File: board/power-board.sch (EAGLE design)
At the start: 365 parts, among them J1 H1, J2 H2, J6 DF13-8P-1.25DS, J7 DF13-10P-1.25DS, J8 DF13-4P-1.25DS, J9 DF13-4P-1.25DS, Q1 TPC8120, Q2 TPC8120, Q3 SI7288, U1 INA214DCK, U10 INA214DCK, U11 INA214DCK, U12 INA214DCK, U13 MCP6561T-E/LT, U14 INA214DCK, U15 SN74AUP1G00DCK, U16 SN74LVC1G373DCK, U17 NTHD4508NT1, U18 MCP6561T-E/LT, U19 INA214DCK, U2 INA214DCK, U20 SN74AUP1G00DCK, U21 SN74LVC1G373DCK, U22 NTHD4508NT1, U23 MCP6561T-E/LT, U24 INA214DCK, U25 SN74AUP1G00DCK, U26 SN74LVC1G373DCK, U27 NTHD4508NT1, U28 MCP6561T-E/LT, U29 INA214DCK, U3 INA214DCK, U30 SN74AUP1G00DCK, U31 SN74LVC1G373DCK, U32 NTHD4508NT1, U33 MCP6561T-E/LT, U34 INA214DCK, U35 SN74AUP1G00DCK, U36 SN74LVC1G373DCK, U37 NTHD4508NT1, U38 MCP6561T-E/LT, U39 INA214DCK, U4 INA214DCK, U40 SN74AUP1T08DCK, U41 SN74LVC1G373DCK, U42 FDS8858CZ, U43 TLV3491AIDBV, U44 TPS62132RGT, U45 FDS8858CZ, U46 TLV3491AIDBV, U47 TPS62133RGT, U48 FDS8858CZ, U49 MSP430F2132, U5 INA214DCK, U50 ADG732, U51 SPV1040T, U52 SPV1040T, U53 BQ24650_RVA_16, U54 INA214DCK, U6 INA214DCK, U7 INA214DCK, U8 INA214DCK, U9 INA214DCK, X1 32.768k

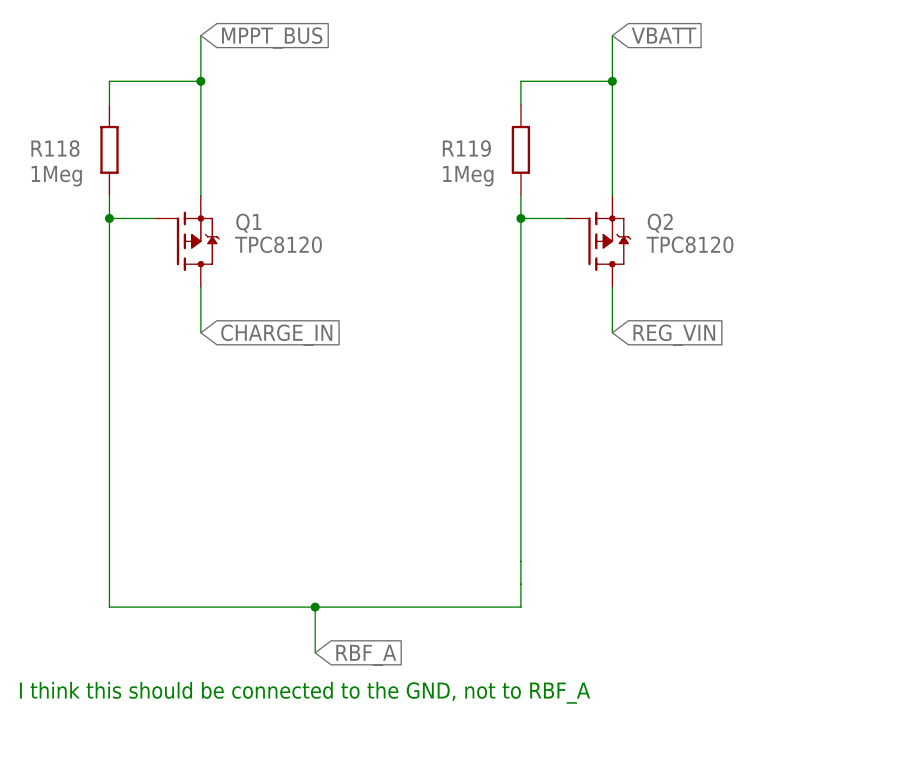
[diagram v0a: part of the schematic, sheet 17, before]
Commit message: removing deployment switches, adding testpoints
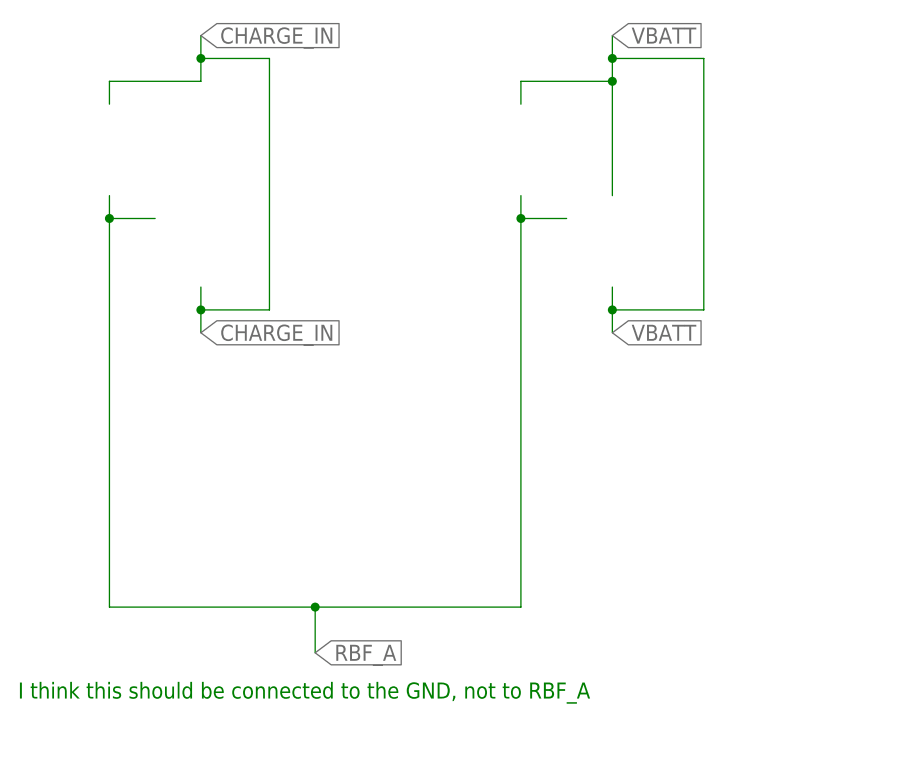
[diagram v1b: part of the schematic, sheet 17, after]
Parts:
- removed Q1, Q2: TPC8120, gdp_pss_library:TPC8120
- removed R118, R119: 1Meg, rcl:R-EU_R0603
- added FID1, FID2, FID3, FID4: FIDUCIAL1X2-STOP, fiducial:FIDUCIAL1X2-STOP
- added TP1, TP10, TP11, TP12, TP13, TP14, TP2, TP3, TP4, TP5, TP6, TP7, TP8, TP9: PTR1TP09R, testpad:PTR1TP09R
- R39: value 442m -> 50m
- R48: value 43m -> 124m
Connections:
- net 3V3_BU_RADIO renamed 5V_TX_RADIO
- removed net MPPT_BUS: C122.1, Q1.S, R113.1, R116.1, R118.2, R31.2
- removed net REG_VIN: C100.1, C104.1, C106.1, C107.1, C95.1, C97.1, C99.1, J2.20, Q2.D, R102.1, R37.2, R44.2, R53.2, R62.2, R71.2, R80.2, R84.1, R95.1, U39.IN+, U44.AVIN, U44.EN, U44.PVIN, U47.AVIN, U47.EN, U47.PVIN
- new net 5V_RX_RADIO: C53.1, R55.2, U22A.S
- net 3V3_RADIO: no longer C53.1, R55.2, U22A.S
- net CHARGE_IN: now also C122.1, R113.1, R116.1, R31.2; no longer Q1.D
- net OCP1_COMP_OUT: now also TP12.TP
- net OCP1_MCU_EN: now also TP11.TP
- net OCP1_SENSEM: now also R44.2
- net OCP2_COMP_OUT: now also TP10.TP
- net OCP2_MCU_EN: now also TP9.TP
- net OCP2_SENSEM: now also R53.2
- net OCP3_COMP_OUT: now also TP8.TP
- net OCP3_MCU_EN: now also TP7.TP
- net OCP3_SENSEM: now also R62.2
- net OCP4_COMP_OUT: now also TP6.TP
- net OCP4_MCU_EN: now also TP5.TP
- net OCP4_SENSEM: now also R71.2
- net OCP5_COMP_OUT: now also TP4.TP
- net OCP5_MCU_EN: now also TP3.TP
- net OCP5_SENSEM: now also R80.2
- net OCP6_COMP_OUT: now also TP2.TP
- net OCP6_MCU_EN: now also TP1.TP
- net RBF_A: no longer Q1.G, Q2.G, R118.1, R119.1
- net UVP3V3_GATE: now also TP13.TP
- net UVP3V3_OUT: no longer R39.1, R48.1, U14.IN+, U19.IN+
- net UVP5V_GATE: now also TP14.TP
- net UVP5V_OUT: now also R39.1, R48.1, U14.IN+, U19.IN+
- net VBATT: now also C100.1, C104.1, C106.1, C107.1, C95.1, C97.1, C99.1, J2.20, R102.1, R37.2, R84.1, R95.1, U39.IN+, U44.AVIN, U44.EN, U44.PVIN, U47.AVIN, U47.EN, U47.PVIN; no longer Q2.S, R119.2

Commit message: done (hopefully)
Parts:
- added TP15, TP16, TP17, TP18, TP19, TP20, TP21, TP22, TP23, TP24, TP25, TP26, TP27, TP28, TP29, TP30: PTR1TP09R, testpad:PTR1TP09R
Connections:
- removed net 3V3_RADIO: J1.51
- net 3V3_FLIGHT_MCU: now also TP24.TP
- net 3V3_SYS: now also TP16.TP
- net 5V_CAMERA: now also TP25.TP
- net 5V_RX_RADIO: now also J1.51, TP26.TP
- net 5V_SYS: now also TP15.TP
- net 5V_TX_RADIO: now also TP27.TP
- net CHARGE_IN: now also TP28.TP
- net GND: now also TP30.TP
- net MPPT2_OUT: now also TP29.TP
- net OCP1_SENSEM: no longer R44.2
- net OCP2_SENSEM: no longer R53.2
- net OCP3_SENSEM: no longer R62.2
- net OCP4_SENSEM: no longer R71.2
- net OCP5_SENSEM: no longer R80.2
- net OEM615_3V3: now also TP23.TP
- net OEM615_LNA_PWR: now also TP22.TP
- net REG3V3: now also TP21.TP
- net REG5V: now also TP20.TP
- net UVP3V3_OUT: now also TP17.TP; no longer C40.1, C51.1
- net UVP5V_OUT: now also C40.1, C51.1, TP18.TP
- net VBATT: now also R44.2, R53.2, R62.2, R71.2, R80.2, TP19.TP

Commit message: committing WIP
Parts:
- added C143, C148, C153, C158: 1u, rcl:C-EUC0603K
- added C144, C149, C154, C159: 100n, rcl:C-EUC0603K
- added C145, C146, C150, C151, C155, C156, C160, C161: 10u, rcl:C-EUC0805K
- added C147, C152, C157, C162: 4.7u, rcl:C-EUC0805K
- added D12, D13, D14, D15: 5V1, diode:SUPPRESSOR-SMBJ
- added L6, L7, L8, L9: 10uH, gdp_pss_library:MSS7341
- added R118, R119, R143, R144, R145, R147, R148, R149, R151, R152, R153, R155: 1k, rcl:R-EU_R0603
- added R142, R146, R150, R154: 10m, rcl:R-EU_R1206
- added TP31, TP32, TP33, TP34, TP35, TP36: PTR1TP09R, testpad:PTR1TP09R
- added U55, U56, U57, U58: SPV1040T, gdp_pss_library:SPV1040T
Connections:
- net MPPT2_OUT renamed MPPT1_MID
- new net MPPT1H_PV_P: C114.1, L3.1, R110.1
- new net MPPT1L_PV_P: C115.1, L4.1, R111.1
- new net MPPT2H_PV_P: C146.1, L6.1, R143.1
- new net MPPT2L_PV_P: C151.1, L7.1, R147.1
- new net MPPT2_MID: C144.2, C145.2, C146.2, C147.2, C150.1, D12.A, R145.1, R146.1, TP32.TP, U55.GND, U55.VCTRL
- new net MPPT3H_PV_P: C156.1, L8.1, R151.1
- new net MPPT3L_PV_P: C161.1, L9.1, R155.1
- new net MPPT3_MID: C154.2, C155.2, C156.2, C157.2, C160.1, D14.A, R153.1, R154.1, TP35.TP, U57.GND, U57.VCTRL
- new net N$778: C144.1, R143.2, U55.MPP-SET, U55.XSHUT
- new net N$779: L6.2, U55.LX
- new net N$780: C148.1, R144.2, U56.ICTRL+
- new net N$781: C148.2, R145.2, U56.ICTRL-
- new net N$782: C152.1, D13.C, R144.1, R146.2, U56.VOUT
- new net N$783: C149.1, R147.2, U56.MPP-SET, U56.XSHUT
- new net N$784: L7.2, U56.LX
- new net N$785: C153.1, R148.2, U57.ICTRL+
- new net N$786: C153.2, R149.2, U57.ICTRL-
- new net N$787: C157.1, D14.C, R148.1, R150.2, U57.VOUT
- new net N$788: C154.1, R151.2, U57.MPP-SET, U57.XSHUT
- new net N$789: L8.2, U57.LX
- new net N$790: C158.1, R152.2, U58.ICTRL+
- new net N$791: C158.2, R153.2, U58.ICTRL-
- new net N$792: C162.1, D15.C, R152.1, R154.2, U58.VOUT
- new net N$793: C159.1, R155.2, U58.MPP-SET, U58.XSHUT
- new net N$794: L9.2, U58.LX
- new net N$89: C143.1, R118.2, U55.ICTRL+
- new net N$91: C143.2, R119.2, U55.ICTRL-
- new net N$92: C147.1, D12.C, R118.1, R142.2, U55.VOUT
- net CHARGE_IN: now also C145.1, C155.1, R119.1, R142.1, R149.1, R150.1, TP31.TP, TP34.TP
- net GND: now also C149.2, C150.2, C151.2, C152.2, C159.2, C160.2, C161.2, C162.2, D13.A, D15.A, TP33.TP, TP36.TP, U56.GND, U56.VCTRL, U58.GND, U58.VCTRL
- net MPPT1_PV_P: no longer C114.1, L3.1, R110.1
- net MPPT2_PV_P: no longer C115.1, L4.1, R111.1
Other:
- note added: "< WHY?"
- note added: "MPPT 1H"
- note added: "MPPT 1L"
- note added: "MPPT 2H"
- note added: "MPPT 2L"
- note added: "MPPT 3H"
- note added: "MPPT 3L"
- note added: "review all these connections"
- note added: "wire thse SWD pins"
- moved on the sheet: C114, C115, C116, C117, C118, C119, C120, C121, C122, C123, D7, D8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

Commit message: various bits of routing over a period of time
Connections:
- net MPPT1H_PV_P: now also R6.2, R9.2, U4.IN-, U5.IN-
- net MPPT1L_PV_P: now also R16.2, R19.2, U10.IN-, U9.IN-
- net MPPT1_MID: no longer J2.16, J2.8, J9.2
- net MPPT1_PV_P: no longer R10.2, R13.2, R5.2, R6.2, R9.2, U3.IN-, U4.IN-, U5.IN-, U6.IN-, U7.IN-
- net MPPT2H_PV_P: now also R10.2, R13.2, U6.IN-, U7.IN-
- net MPPT2L_PV_P: now also R20.2, R23.2, U11.IN-, U12.IN-
- net MPPT2_MID: now also J2.16, J9.2
- net MPPT2_PV_P: no longer R15.2, R16.2, R19.2, R20.2, R23.2, U10.IN-, U11.IN-, U12.IN-, U8.IN-, U9.IN-
- net MPPT3H_PV_P: now also R5.2, U3.IN-
- net MPPT3L_PV_P: now also R15.2, U8.IN-
- net MPPT3_MID: now also J2.8
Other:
- note added: "1 +"
- note added: "1 -"
- note added: "2 +"
- note added: "2 -"
- note added: "east pv 1 +"
- note added: "east pv 1 -"
- note added: "east pv 2 +"
- note added: "east pv 2 -"
- note added: "east/west"
- note added: "north/south"
- note added: "top"
- note added: "top pv 1 +"
- note added: "top pv 1 -"
- note added: "top pv 2 +"
- note added: "top pv 2 -"
- note removed: "< WHY?"

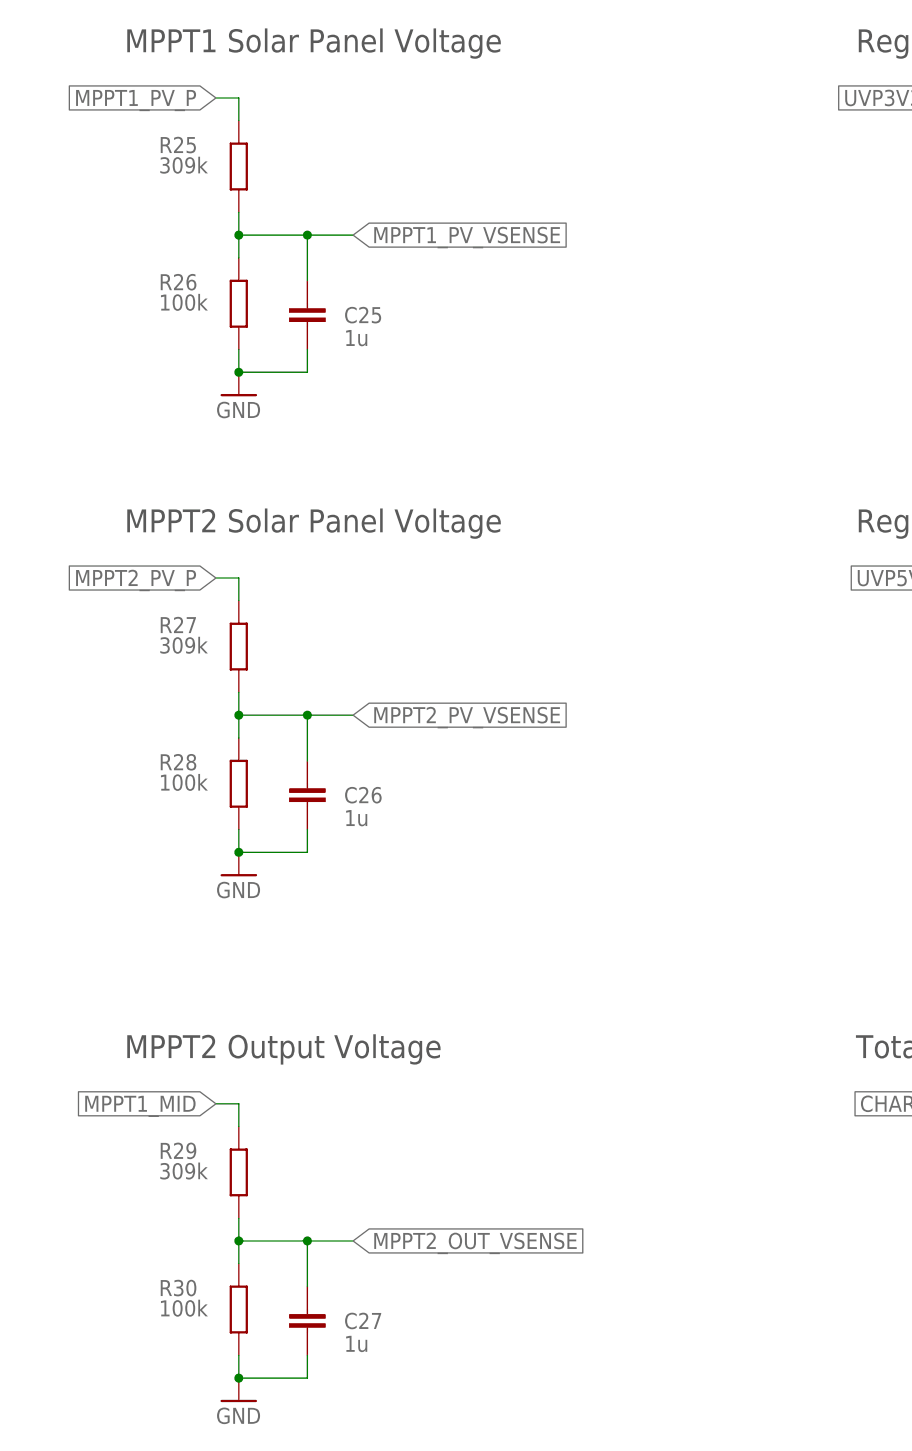
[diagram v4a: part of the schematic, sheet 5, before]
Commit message: changing mppt voltage monitoring points
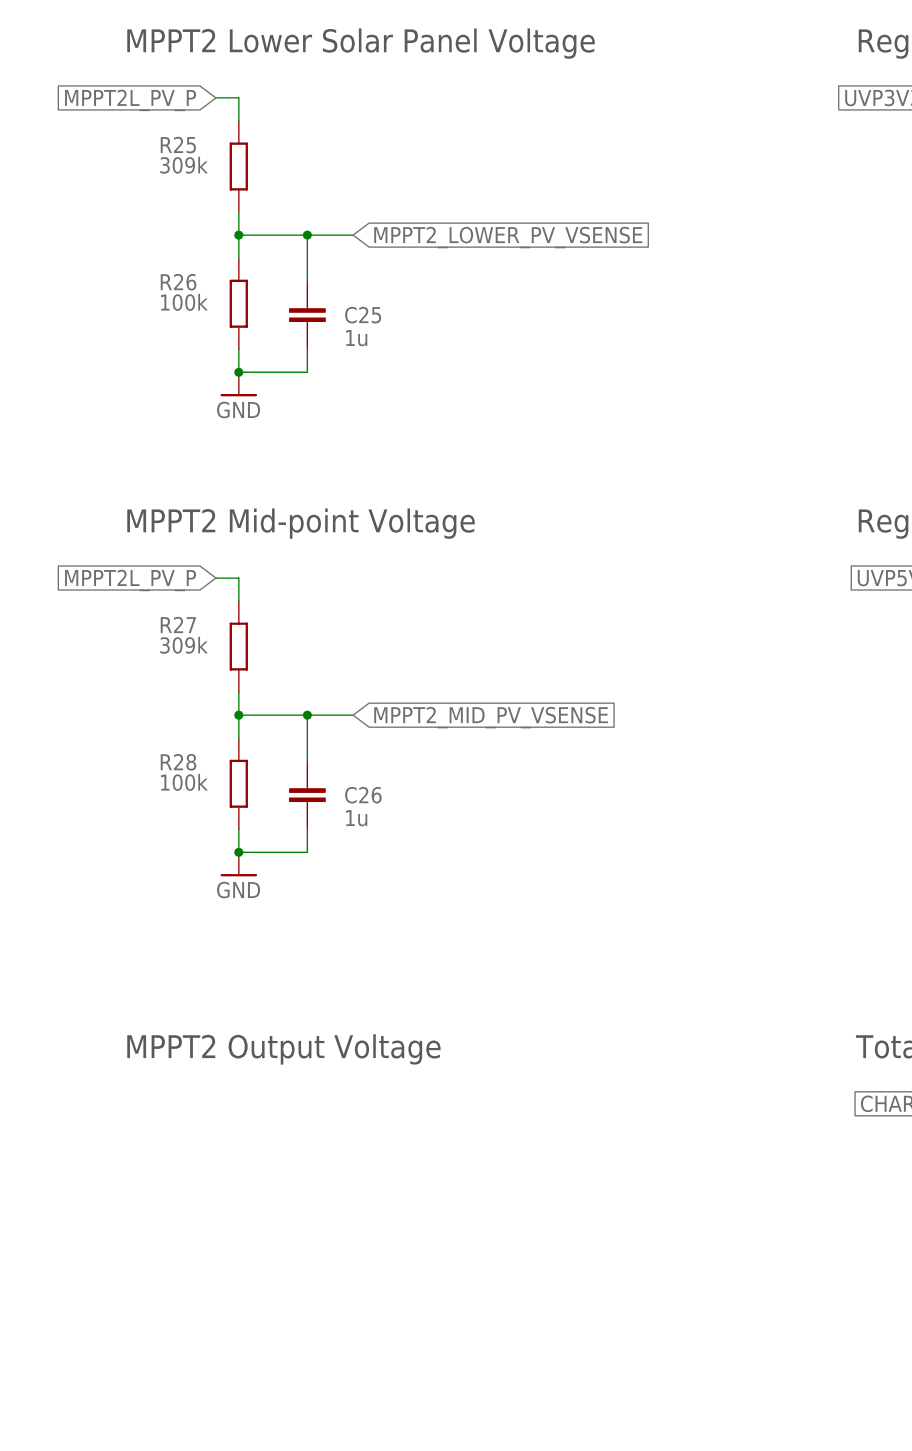
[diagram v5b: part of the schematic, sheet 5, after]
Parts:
- removed C27: 1u, rcl:C-EUC0603
- removed R29: 309k, rcl:R-EU_R0603
- removed R30: 100k, rcl:R-EU_R0603
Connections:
- net MPPT1_PV_VSENSE renamed MPPT2_LOWER_PV_VSENSE
- net MPPT2_PV_VSENSE renamed MPPT2_MID_PV_VSENSE
- removed net MPPT1_PV_P: R25.2
- removed net MPPT2_OUT_VSENSE: C27.1, R29.1, R30.2
- removed net MPPT2_PV_P: R27.2
- net GND: no longer C27.2, R30.1
- net MPPT1_MID: no longer R29.2
- net MPPT2L_PV_P: now also R25.2, R27.2
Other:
- note added: "MPPT2 Lower Solar Panel Voltage"
- note added: "MPPT2 Mid-point Voltage"
- note removed: "MPPT1 Solar Panel Voltage"
- note removed: "MPPT2 Solar Panel Voltage"
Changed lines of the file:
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@@
 <?xml version="1.0" encoding="utf-8"?>
 <!DOCTYPE eagle SYSTEM "eagle.dtd">
-<eagle version="7.6.0">
+<eagle version="9.0.1">
 <drawing>
 <settings>
-<setting alwaysvectorfont="yes"/>
+<setting alwaysvectorfont="no"/>
+<setting keepoldvectorfont="yes"/>
 <setting verticaltext="up"/>
 </settings>
@@
 <part name="C19" library="rcl" deviceset="C-EU" device="C0603" value="100n"/>
 <part name="GND23" library="supply1" deviceset="GND" device=""/>
-<part name="R29" library="rcl" deviceset="R-EU_" device="R0603" value="309k"/>
-<part name="R30" library="rcl" deviceset="R-EU_" device="R0603" value="100k"/>
-<part name="GND31" library="supply1" deviceset="GND" device=""/>
 <part name="R21" library="rcl" deviceset="R-EU_" device="R0603" value="10k"/>
 <part name="C21" library="rcl" deviceset="C-EU" device="C0603" value="1u"/>
 <part name="GND25" library="supply1" deviceset="GND" device=""/>
-<part name="C27" library="rcl" deviceset="C-EU" device="C0603" value="1u"/>
 <part name="J7" library="con-hirose-df13" deviceset="DF13-10P-1.25" device="DS"/>
 <part name="J6" library="con-hirose-df13" deviceset="DF13-8P-1.25" device="DS"/>
@@
 <description>Voltage Measurements</description>
 <plain>
-<text x="27.94" y="162.56" size="2.54" layer="97">MPPT1 Solar Panel Voltage</text>
-<text x="27.94" y="109.22" size="2.54" layer="97">MPPT2 Solar Panel Voltage</text>
+<text x="27.94" y="162.56" size="2.54" layer="97">MPPT2 Lower Solar Panel Voltage</text>
+<text x="27.94" y="109.22" size="2.54" layer="97">MPPT2 Mid-point Voltage</text>
 <text x="109.22" y="109.22" size="2.54" layer="97">Regulated 5V After UVP Switch</text>
 <text x="109.22" y="162.56" size="2.54" layer="97">Regulated 3V3 After UVP Switch</text>
@@
 </instance>
 <instance part="FRAME5" gate="G$1" x="0" y="0"/>
-<instance part="R29" gate="G$1" x="40.64" y="38.1" smashed="yes" rot="R90">
-<attribute name="NAME" x="31.75" y="39.5986" size="1.778" layer="95"/>
-<attribute name="VALUE" x="31.75" y="37.338" size="1.778" layer="96"/>
-</instance>
-<instance part="R30" gate="G$1" x="40.64" y="22.86" smashed="yes" rot="R90">
-<attribute name="NAME" x="31.75" y="24.3586" size="1.778" layer="95"/>
-<attribute name="VALUE" x="31.75" y="22.098" size="1.778" layer="96"/>
-</instance>
-<instance part="GND31" gate="1" x="40.64" y="12.7"/>
-<instance part="C27" gate="G$1" x="48.26" y="22.86" smashed="yes">
-<attribute name="NAME" x="52.324" y="20.701" size="1.778" layer="95"/>
-<attribute name="VALUE" x="52.324" y="18.161" size="1.778" layer="96"/>
-</instance>
 <instance part="R31" gate="G$1" x="127" y="38.1" smashed="yes" rot="R90">
 <attribute name="NAME" x="118.11" y="39.5986" size="1.778" layer="95"/>
@@
 </segment>
 <segment>
-<pinref part="GND31" gate="1" pin="GND"/>
-<pinref part="R30" gate="G$1" pin="1"/>
-<wire x1="40.64" y1="15.24" x2="40.64" y2="17.78" width="0.1524" layer="91"/>
-<pinref part="C27" gate="G$1" pin="2"/>
-<wire x1="48.26" y1="17.78" x2="48.26" y2="15.24" width="0.1524" layer="91"/>
-<wire x1="48.26" y1="15.24" x2="40.64" y2="15.24" width="0.1524" layer="91"/>
-<junction x="40.64" y="15.24"/>
-</segment>
-<segment>
 <pinref part="GND32" gate="1" pin="GND"/>
 <pinref part="R32" gate="G$1" pin="1"/>
@@
 </segment>
 </net>
-<net name="MPPT1_PV_P" class="0">
-<segment>
-<label x="38.1" y="157.48" size="1.778" layer="95" rot="R180" xref="yes"/>
-<pinref part="R25" gate="G$1" pin="2"/>
-<wire x1="40.64" y1="157.48" x2="38.1" y2="157.48" width="0.1524" layer="91"/>
-<wire x1="40.64" y1="154.94" x2="40.64" y2="157.48" width="0.1524" layer="91"/>
-</segment>
-</net>
-<net name="MPPT1_PV_VSENSE" class="0">
+<net name="MPPT2_LOWER_PV_VSENSE" class="0">
 <segment>
 <pinref part="R26" gate="G$1" pin="2"/>
@@
 </segment>
 </net>
-<net name="MPPT2_PV_P" class="0">
+<net name="MPPT2L_PV_P" class="0">
 <segment>
 <label x="38.1" y="104.14" size="1.778" layer="95" rot="R180" xref="yes"/>
@@
 <wire x1="40.64" y1="101.6" x2="40.64" y2="104.14" width="0.1524" layer="91"/>
 </segment>
+<segment>
+<label x="38.1" y="157.48" size="1.778" layer="95" rot="R180" xref="yes"/>
+<pinref part="R25" gate="G$1" pin="2"/>
+<wire x1="40.64" y1="157.48" x2="38.1" y2="157.48" width="0.1524" layer="91"/>
+<wire x1="40.64" y1="154.94" x2="40.64" y2="157.48" width="0.1524" layer="91"/>
+</segment>
 </net>
-<net name="MPPT2_PV_VSENSE" class="0">
+<net name="MPPT2_MID_PV_VSENSE" class="0">
 <segment>
 <pinref part="R28" gate="G$1" pin="2"/>
@@
 </segment>
 </net>
-<net name="MPPT1_MID" class="0">
-<segment>
-<label x="38.1" y="45.72" size="1.778" layer="95" rot="R180" xref="yes"/>
-<pinref part="R29" gate="G$1" pin="2"/>
-<wire x1="40.64" y1="45.72" x2="38.1" y2="45.72" width="0.1524" layer="91"/>
-<wire x1="40.64" y1="43.18" x2="40.64" y2="45.72" width="0.1524" layer="91"/>
-</segment>
-</net>
-<net name="MPPT2_OUT_VSENSE" class="0">
-<segment>
-<pinref part="R30" gate="G$1" pin="2"/>
-<pinref part="R29" gate="G$1" pin="1"/>
-<wire x1="40.64" y1="27.94" x2="40.64" y2="30.48" width="0.1524" layer="91"/>
-<wire x1="40.64" y1="30.48" x2="40.64" y2="33.02" width="0.1524" layer="91"/>
-<wire x1="40.64" y1="30.48" x2="48.26" y2="30.48" width="0.1524" layer="91"/>
-<label x="53.34" y="30.48" size="1.778" layer="95" xref="yes"/>
-<junction x="40.64" y="30.48"/>
-<pinref part="C27" gate="G$1" pin="1"/>
-<wire x1="48.26" y1="30.48" x2="53.34" y2="30.48" width="0.1524" layer="91"/>
-<wire x1="48.26" y1="25.4" x2="48.26" y2="30.48" width="0.1524" layer="91"/>
-<junction x="48.26" y="30.48"/>
-</segment>
-</net>
 <net name="CHARGE_IN" class="0">
 <segment>
@@
 </segment>
 </net>
-<net name="MPPT1_PV_VSENSE" class="0">
+<net name="MPPT2_LOWER_PV_VSENSE" class="0">
 <segment>
 <label x="198.12" y="106.68" size="1.27" layer="95" xref="yes"/>
@@
 </segment>
 </net>
-<net name="MPPT2_PV_VSENSE" class="0">
+<net name="MPPT2_MID_PV_VSENSE" class="0">
 <segment>
 <label x="198.12" y="104.14" size="1.27" layer="95" xref="yes"/>
